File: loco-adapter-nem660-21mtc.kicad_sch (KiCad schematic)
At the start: 9 parts, among them J701 Conn_02x11_Odd_Even

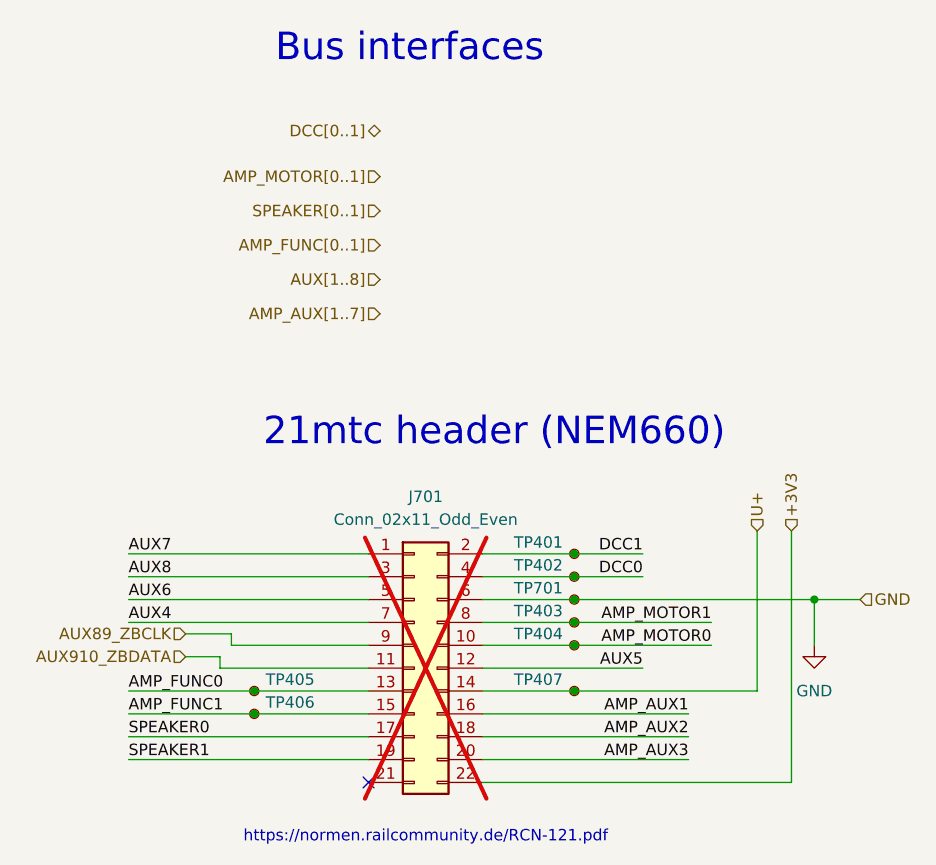
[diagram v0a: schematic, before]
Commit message: Fix - Remove ERC error, refresh annotation
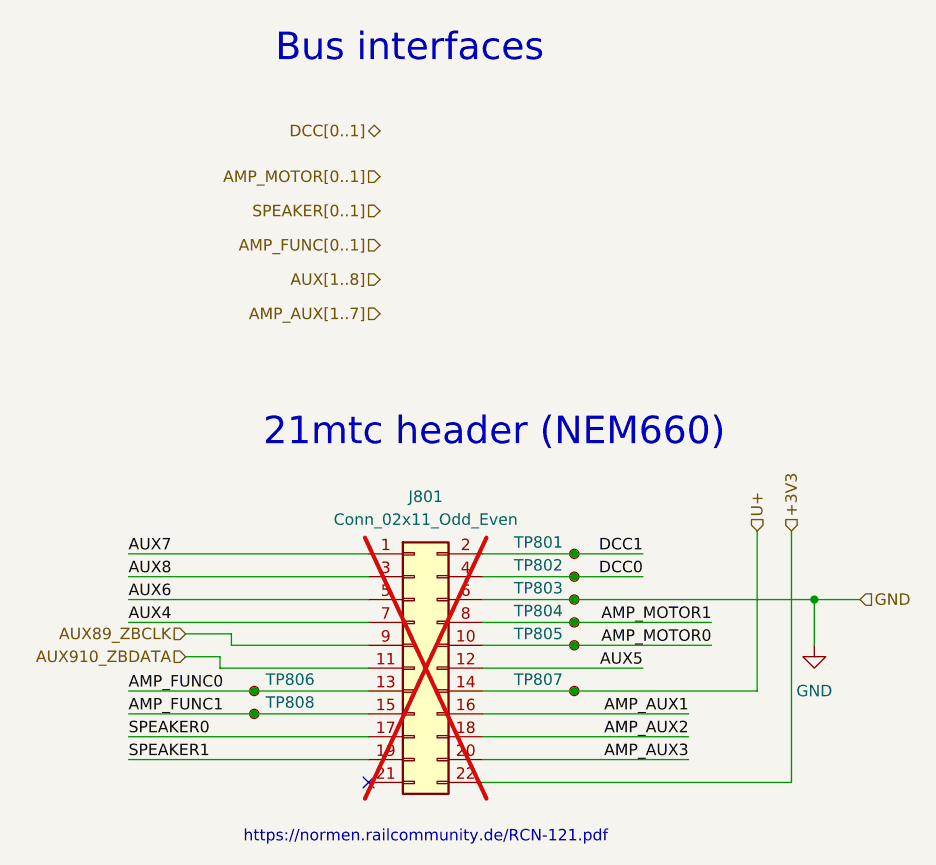
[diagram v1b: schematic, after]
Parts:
- renumbered J701 to J801, TP401 to TP801, TP402 to TP802, TP701 to TP803, TP403 to TP804, TP404 to TP805, TP405 to TP806, TP407 to TP807, TP406 to TP808
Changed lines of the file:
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@@
 		(on_board yes)
 		(dnp no)
-		(property "Reference" "TP403"
+		(property "Reference" "TP804"
 			(at 74.93 86.3599 0)
 			(effects
@@
 			(project "xDuinoRails-Thor-M"
 				(path "/fb33ec4e-6596-45d2-a121-8d3475acd69a/3c699e35-5808-46af-b922-4c3eb1f6da5c"
-					(reference "TP403")
+					(reference "TP804")
 					(unit 1)
 				)
@@
 		(on_board yes)
 		(dnp no)
-		(property "Reference" "TP406"
+		(property "Reference" "TP808"
 			(at 41.91 96.5199 0)
 			(effects
@@
 			(project "xDuinoRails-Thor-M"
 				(path "/fb33ec4e-6596-45d2-a121-8d3475acd69a/3c699e35-5808-46af-b922-4c3eb1f6da5c"
-					(reference "TP406")
+					(reference "TP808")
 					(unit 1)
 				)
@@
 		(on_board yes)
 		(dnp no)
-		(property "Reference" "TP407"
+		(property "Reference" "TP807"
 			(at 74.93 93.9799 0)
 			(effects
@@
 			(project "xDuinoRails-Thor-M"
 				(path "/fb33ec4e-6596-45d2-a121-8d3475acd69a/3c699e35-5808-46af-b922-4c3eb1f6da5c"
-					(reference "TP407")
+					(reference "TP807")
 					(unit 1)
 				)
@@
 		(on_board yes)
 		(dnp no)
-		(property "Reference" "TP701"
+		(property "Reference" "TP803"
 			(at 74.93 83.8199 0)
 			(effects
@@
 			(project "xDuinoRails-Thor-M"
 				(path "/fb33ec4e-6596-45d2-a121-8d3475acd69a/3c699e35-5808-46af-b922-4c3eb1f6da5c"
-					(reference "TP701")
+					(reference "TP803")
 					(unit 1)
 				)
@@
 		(on_board yes)
 		(dnp no)
-		(property "Reference" "TP402"
+		(property "Reference" "TP802"
 			(at 74.93 81.2799 0)
 			(effects
@@
 			(project "xDuinoRails-Thor-M"
 				(path "/fb33ec4e-6596-45d2-a121-8d3475acd69a/3c699e35-5808-46af-b922-4c3eb1f6da5c"
-					(reference "TP402")
+					(reference "TP802")
 					(unit 1)
 				)
@@
 		(dnp yes)
 		(fields_autoplaced yes)
-		(property "Reference" "J701"
+		(property "Reference" "J801"
 			(at 59.69 73.66 0)
 			(effects
@@
 			(project ""
 				(path "/fb33ec4e-6596-45d2-a121-8d3475acd69a/3c699e35-5808-46af-b922-4c3eb1f6da5c"
-					(reference "J701")
+					(reference "J801")
 					(unit 1)
 				)
@@
 		(on_board yes)
 		(dnp no)
-		(property "Reference" "TP404"
+		(property "Reference" "TP805"
 			(at 74.93 88.8999 0)
 			(effects
@@
 			(project "xDuinoRails-Thor-M"
 				(path "/fb33ec4e-6596-45d2-a121-8d3475acd69a/3c699e35-5808-46af-b922-4c3eb1f6da5c"
-					(reference "TP404")
+					(reference "TP805")
 					(unit 1)
 				)
@@
 		(on_board yes)
 		(dnp no)
-		(property "Reference" "TP405"
+		(property "Reference" "TP806"
 			(at 41.91 93.9799 0)
 			(effects
@@
 			(project "xDuinoRails-Thor-M"
 				(path "/fb33ec4e-6596-45d2-a121-8d3475acd69a/3c699e35-5808-46af-b922-4c3eb1f6da5c"
-					(reference "TP405")
+					(reference "TP806")
 					(unit 1)
 				)
@@
 		(on_board yes)
 		(dnp no)
-		(property "Reference" "TP401"
+		(property "Reference" "TP801"
 			(at 74.93 78.7399 0)
 			(effects
@@
 			(project "xDuinoRails-Thor-M"
 				(path "/fb33ec4e-6596-45d2-a121-8d3475acd69a/3c699e35-5808-46af-b922-4c3eb1f6da5c"
-					(reference "TP401")
+					(reference "TP801")
 					(unit 1)
 				)
@@
 			(project "loco-adapter-nem660-21mtc"
 				(path "/fb33ec4e-6596-45d2-a121-8d3475acd69a/3c699e35-5808-46af-b922-4c3eb1f6da5c"
-					(reference "#PWR701")
-					(unit 1)
-				)
+					(reference "#PWR801")
+					(unit 1)
+				)

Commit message: Fix - revert to working model
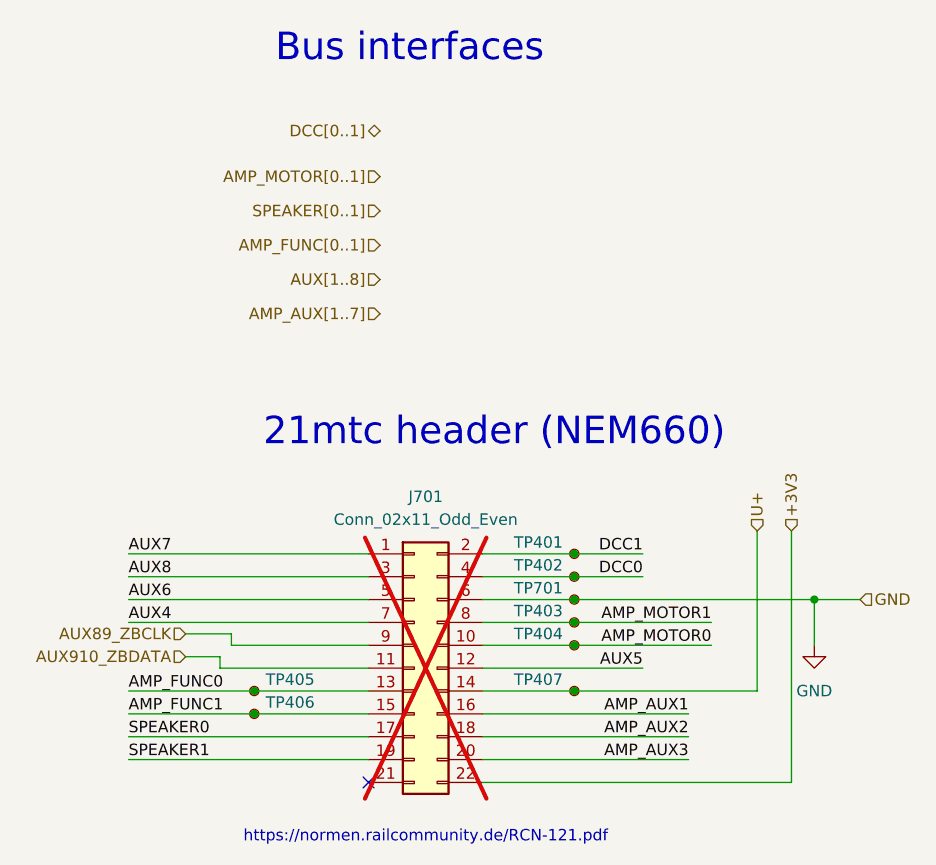
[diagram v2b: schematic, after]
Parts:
- renumbered J801 to J701, TP801 to TP401, TP802 to TP402, TP804 to TP403, TP805 to TP404, TP806 to TP405, TP808 to TP406, TP807 to TP407, TP803 to TP701
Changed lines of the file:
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@@
 		(on_board yes)
 		(dnp no)
-		(property "Reference" "TP804"
+		(property "Reference" "TP403"
 			(at 74.93 86.3599 0)
 			(effects
@@
 			(project "xDuinoRails-Thor-M"
 				(path "/fb33ec4e-6596-45d2-a121-8d3475acd69a/3c699e35-5808-46af-b922-4c3eb1f6da5c"
-					(reference "TP804")
+					(reference "TP403")
 					(unit 1)
 				)
@@
 		(on_board yes)
 		(dnp no)
-		(property "Reference" "TP808"
+		(property "Reference" "TP406"
 			(at 41.91 96.5199 0)
 			(effects
@@
 			(project "xDuinoRails-Thor-M"
 				(path "/fb33ec4e-6596-45d2-a121-8d3475acd69a/3c699e35-5808-46af-b922-4c3eb1f6da5c"
-					(reference "TP808")
+					(reference "TP406")
 					(unit 1)
 				)
@@
 		(on_board yes)
 		(dnp no)
-		(property "Reference" "TP807"
+		(property "Reference" "TP407"
 			(at 74.93 93.9799 0)
 			(effects
@@
 			(project "xDuinoRails-Thor-M"
 				(path "/fb33ec4e-6596-45d2-a121-8d3475acd69a/3c699e35-5808-46af-b922-4c3eb1f6da5c"
-					(reference "TP807")
+					(reference "TP407")
 					(unit 1)
 				)
@@
 		(on_board yes)
 		(dnp no)
-		(property "Reference" "TP803"
+		(property "Reference" "TP701"
 			(at 74.93 83.8199 0)
 			(effects
@@
 			(project "xDuinoRails-Thor-M"
 				(path "/fb33ec4e-6596-45d2-a121-8d3475acd69a/3c699e35-5808-46af-b922-4c3eb1f6da5c"
-					(reference "TP803")
+					(reference "TP701")
 					(unit 1)
 				)
@@
 		(on_board yes)
 		(dnp no)
-		(property "Reference" "TP802"
+		(property "Reference" "TP402"
 			(at 74.93 81.2799 0)
 			(effects
@@
 			(project "xDuinoRails-Thor-M"
 				(path "/fb33ec4e-6596-45d2-a121-8d3475acd69a/3c699e35-5808-46af-b922-4c3eb1f6da5c"
-					(reference "TP802")
+					(reference "TP402")
 					(unit 1)
 				)
@@
 		(dnp yes)
 		(fields_autoplaced yes)
-		(property "Reference" "J801"
+		(property "Reference" "J701"
 			(at 59.69 73.66 0)
 			(effects
@@
 			(project ""
 				(path "/fb33ec4e-6596-45d2-a121-8d3475acd69a/3c699e35-5808-46af-b922-4c3eb1f6da5c"
-					(reference "J801")
+					(reference "J701")
 					(unit 1)
 				)
@@
 		(on_board yes)
 		(dnp no)
-		(property "Reference" "TP805"
+		(property "Reference" "TP404"
 			(at 74.93 88.8999 0)
 			(effects
@@
 			(project "xDuinoRails-Thor-M"
 				(path "/fb33ec4e-6596-45d2-a121-8d3475acd69a/3c699e35-5808-46af-b922-4c3eb1f6da5c"
-					(reference "TP805")
+					(reference "TP404")
 					(unit 1)
 				)
@@
 		(on_board yes)
 		(dnp no)
-		(property "Reference" "TP806"
+		(property "Reference" "TP405"
 			(at 41.91 93.9799 0)
 			(effects
@@
 			(project "xDuinoRails-Thor-M"
 				(path "/fb33ec4e-6596-45d2-a121-8d3475acd69a/3c699e35-5808-46af-b922-4c3eb1f6da5c"
-					(reference "TP806")
+					(reference "TP405")
 					(unit 1)
 				)
@@
 		(on_board yes)
 		(dnp no)
-		(property "Reference" "TP801"
+		(property "Reference" "TP401"
 			(at 74.93 78.7399 0)
 			(effects
@@
 			(project "xDuinoRails-Thor-M"
 				(path "/fb33ec4e-6596-45d2-a121-8d3475acd69a/3c699e35-5808-46af-b922-4c3eb1f6da5c"
-					(reference "TP801")
+					(reference "TP401")
 					(unit 1)
 				)
@@
 			(project "loco-adapter-nem660-21mtc"
 				(path "/fb33ec4e-6596-45d2-a121-8d3475acd69a/3c699e35-5808-46af-b922-4c3eb1f6da5c"
-					(reference "#PWR801")
-					(unit 1)
-				)
+					(reference "#PWR701")
+					(unit 1)
+				)
